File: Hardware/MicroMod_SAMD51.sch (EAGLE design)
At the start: 30 parts, among them J2 MICROMOD-2222, U1 W25QXX6X5, U2 ATSAMD51J20A-A, Y1 32.768kHz

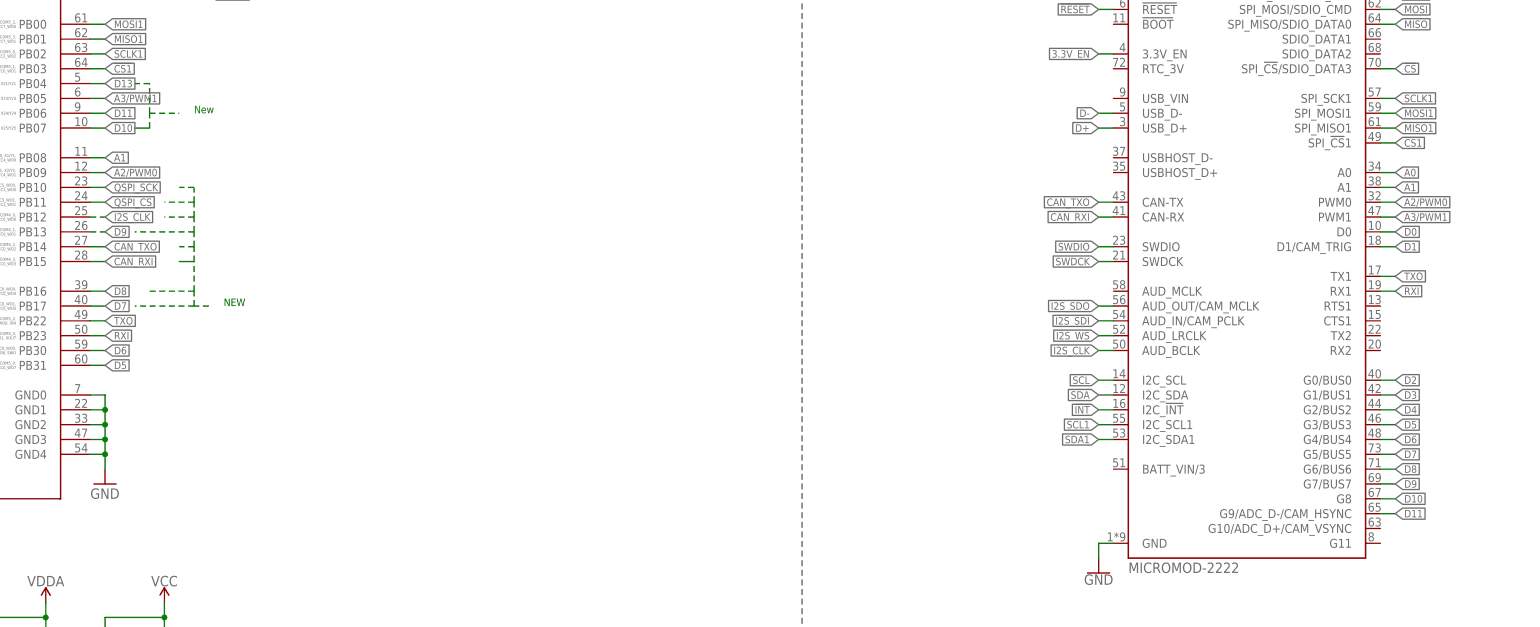
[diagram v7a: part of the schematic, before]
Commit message: More trace routing
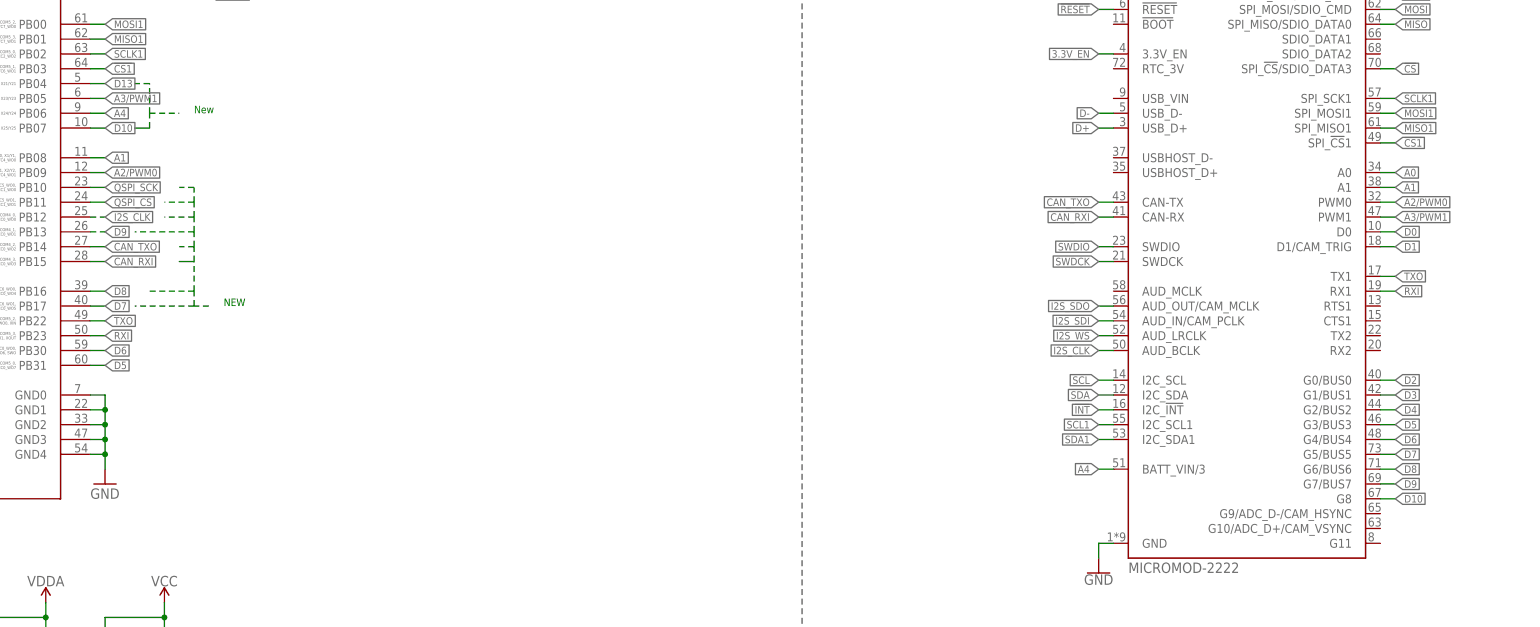
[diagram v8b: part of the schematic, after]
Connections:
- removed net D11: J2.G9/ADC_D-/CAM_HSYNC, U2.PB06
- new net A4: J2.BATT_VIN/3, U2.PB06
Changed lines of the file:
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@@
-</segment>
-</net>
-<net name="D11" class="0">
-<segment>
-<pinref part="J2" gate="J1" pin="G9/ADC_D-/CAM_HSYNC"/>
-<wire x1="373.38" y1="157.48" x2="375.92" y2="157.48" width="0.1524" layer="91"/>
-<label x="375.92" y="157.48" size="1.27" layer="95" xref="yes"/>
-</segment>
-<segment>
-<pinref part="U2" gate="G$1" pin="PB06"/>
-<wire x1="152.4" y1="226.06" x2="154.94" y2="226.06" width="0.1524" layer="91"/>
-<label x="154.94" y="226.06" size="1.27" layer="95" xref="yes"/>
 </segment>
 </net>
@@
 </segment>
 </net>
+<net name="A4" class="0">
+<segment>
+<pinref part="J2" gate="J1" pin="BATT_VIN/3"/>
+<wire x1="327.66" y1="165.1" x2="325.12" y2="165.1" width="0.1524" layer="91"/>
+<label x="325.12" y="165.1" size="1.27" layer="95" rot="R180" xref="yes"/>
+</segment>
+<segment>
+<pinref part="U2" gate="G$1" pin="PB06"/>
+<wire x1="152.4" y1="226.06" x2="154.94" y2="226.06" width="0.1524" layer="91"/>
+<label x="154.94" y="226.06" size="1.27" layer="95" xref="yes"/>
+</segment>
+</net>
